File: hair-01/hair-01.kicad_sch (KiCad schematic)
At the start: 28 parts, among them J1 TYPE-C-31-M-12, Q1 BC847, Q2 BC847, SW1 SW_Push, U1 ESP-12F, U2 AP2112K-3.3, U3 CP2102N-Axx-xQFN24

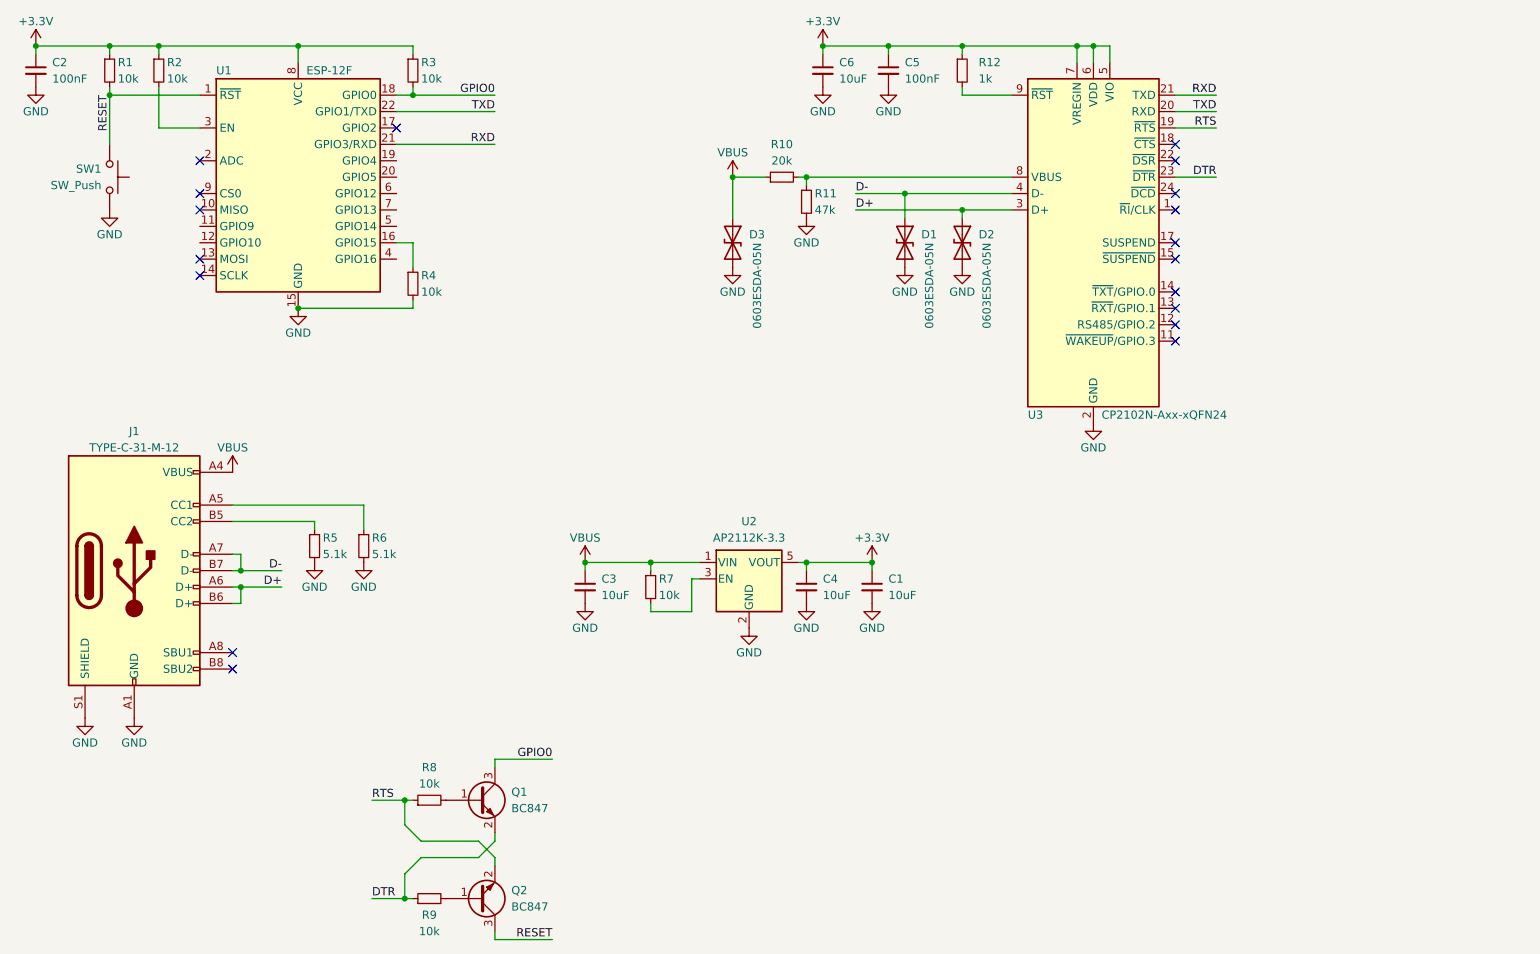
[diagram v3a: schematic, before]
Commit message: hair-01: Add TSMP58000
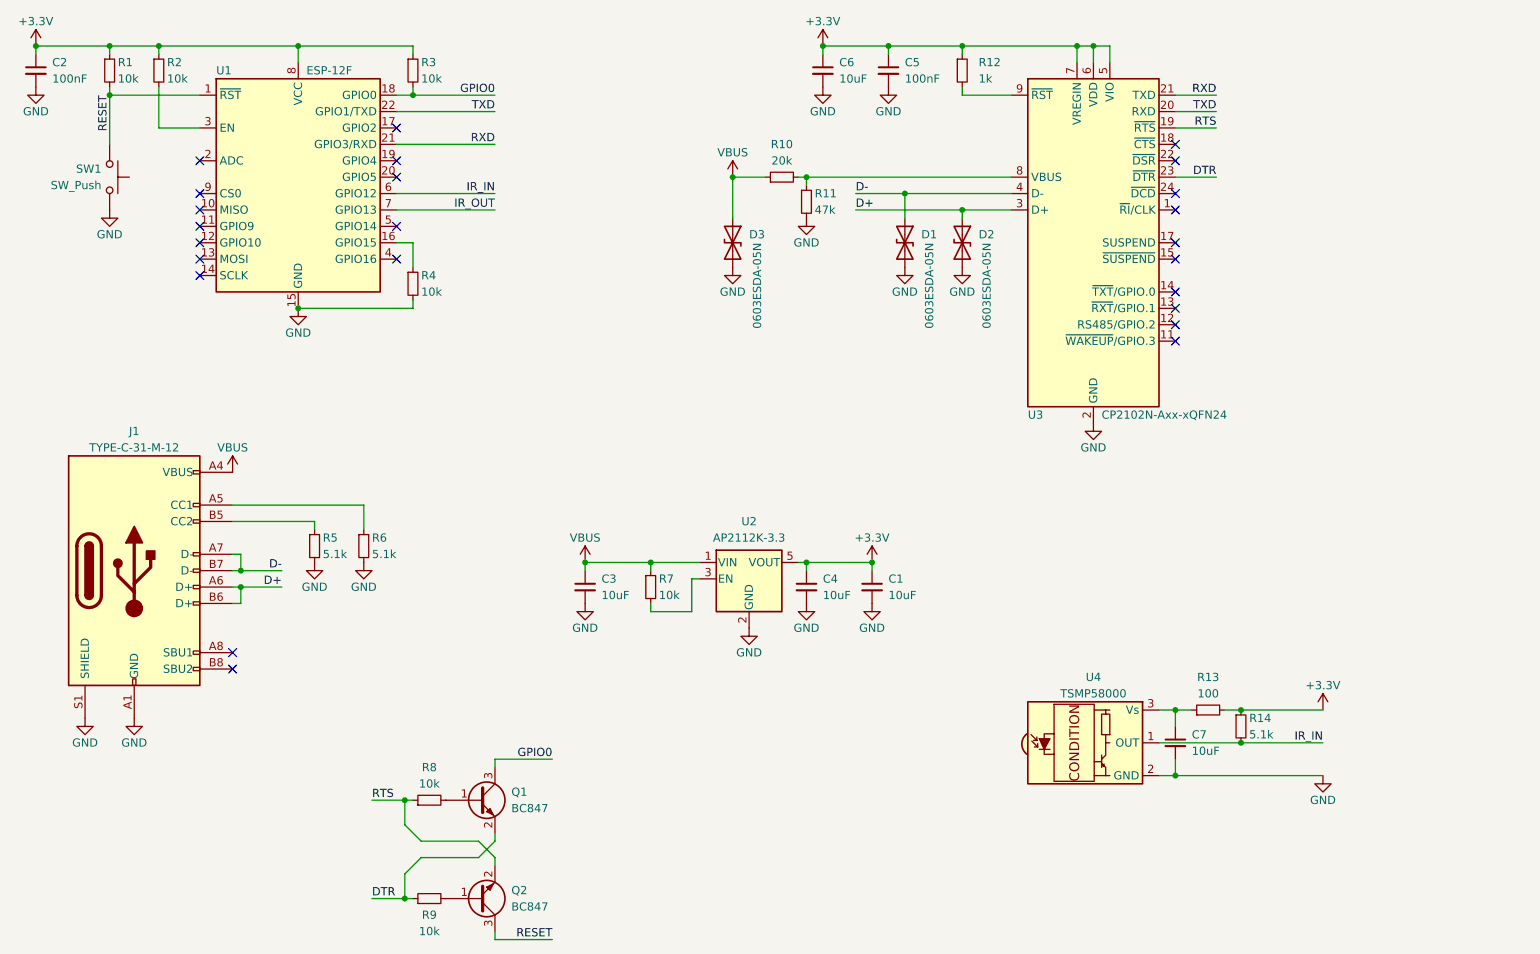
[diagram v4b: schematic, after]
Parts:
- added C7: 10uF, Capacitor_SMD:C_1206_3216Metric, symbol Device:C_Small
- added R13: 100, Resistor_SMD:R_0603_1608Metric, symbol Device:R_Small
- added R14: 5.1k, Resistor_SMD:R_0603_1608Metric, symbol Device:R_Small
- added U4: TSMP58000, OptoDevice:Vishay_MINICAST-3Pin, symbol Interface_Optical:TSMP58000
- C2, C5: footprint Capacitor_SMD:C_0805_2012Metric -> Capacitor_SMD:C_0603_1608Metric; LCSC C49678 -> C14663
- Q1, Q2: LCSC C2762211 -> C2150
- R1, R2, R3, R4, R7, R8, R9: footprint Resistor_SMD:R_0805_2012Metric -> Resistor_SMD:R_0603_1608Metric; LCSC C17414 -> C25804
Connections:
- net +3V3: now also R13.2, R14.1
- net GND: now also C7.2, U4.2 (GND)
- net IR_IN: now reaches U1.6 (GPIO12)
- net IR_IN: now also R14.2, U4.1 (OUT)
- net IR_OUT: now reaches U1.7 (GPIO13)
- new net: C7.1, R13.1, U4.3 (Vs)
- no-connect marks 18 -> 24

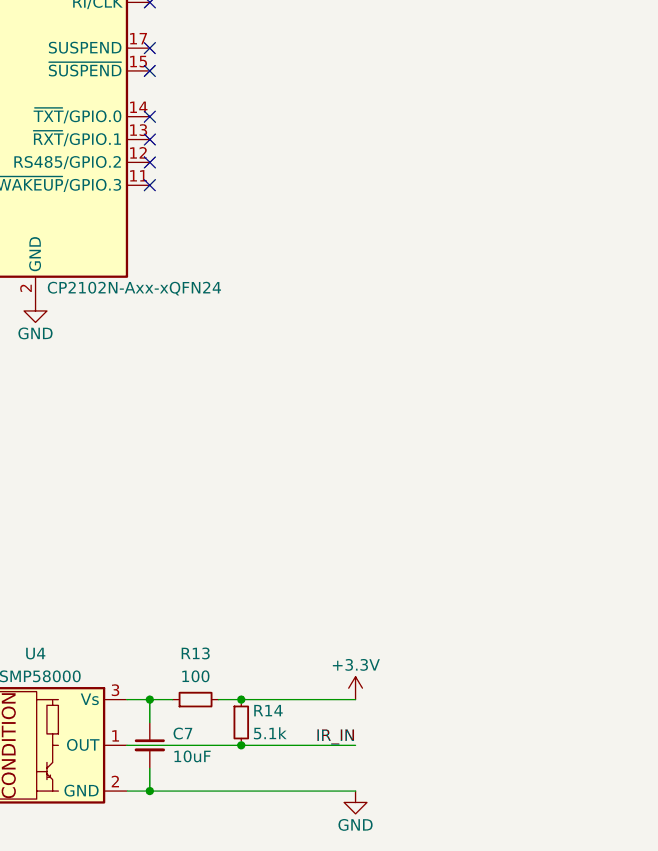
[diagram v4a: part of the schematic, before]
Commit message: hair-01: Add IR output
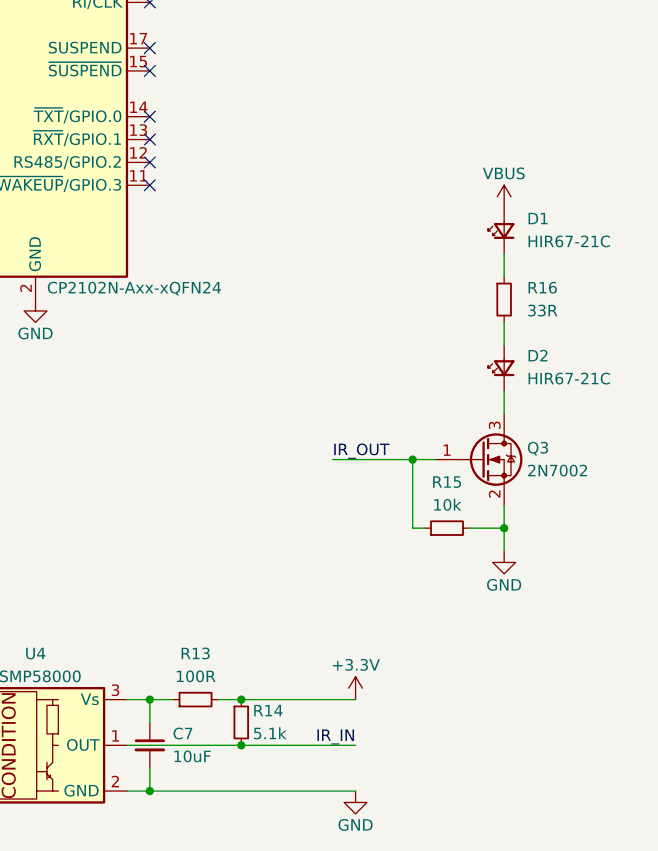
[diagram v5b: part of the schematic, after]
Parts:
- added D1, D2: HIR67-21C, LED_SMD:LED_1210_3225Metric_Pad1.42x2.65mm_HandSolder, symbol Device:LED_Small
- added Q3: 2N7002, Package_TO_SOT_SMD:SOT-23, symbol Transistor_FET:2N7002
- added R15: 10k, Resistor_SMD:R_0603_1608Metric, symbol Device:R_Small
- added R16: 33R, Resistor_SMD:R_1206_3216Metric, symbol Device:R_Small
- R13: value 100 -> 100R
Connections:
- net GND: now also Q3.2 (S), R15.2
- net IR_OUT: now also Q3.1 (G), R15.1
- net VBUS: now also D1.2 (A)
- new net: D1.1 (K), R16.1
- new net: D2.2 (A), R16.2
- new net: D2.1 (K), Q3.3 (D)

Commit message: hair-01: Fix small naming mistake
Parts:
- renumbered D1 to D4, D2 to D5
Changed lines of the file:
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@@
   (symbol (lib_id "Device:LED_Small") (at 251.46 104.14 90) (unit 1)
     (in_bom yes) (on_board yes) (fields_autoplaced)
-    (property "Reference" "D2" (id 0) (at 254 102.8064 90)
+    (property "Reference" "D5" (id 0) (at 254 102.8064 90)
       (effects (font (size 1.27 1.27)) (justify right))
     )
@@
   (symbol (lib_id "power:GND") (at 234.95 151.13 0) (unit 1)
     (in_bom yes) (on_board yes)
-    (property "Reference" "#PWR?" (id 0) (at 234.95 157.48 0)
+    (property "Reference" "#PWR0126" (id 0) (at 234.95 157.48 0)
       (effects (font (size 1.27 1.27)) hide)
     )
@@
   (symbol (lib_id "power:VBUS") (at 251.46 86.36 0) (unit 1)
     (in_bom yes) (on_board yes)
-    (property "Reference" "#PWR?" (id 0) (at 251.46 90.17 0)
+    (property "Reference" "#PWR0127" (id 0) (at 251.46 90.17 0)
       (effects (font (size 1.27 1.27)) hide)
     )
@@
   (symbol (lib_id "power:+3.3V") (at 234.95 140.97 0) (unit 1)
     (in_bom yes) (on_board yes)
-    (property "Reference" "#PWR?" (id 0) (at 234.95 144.78 0)
+    (property "Reference" "#PWR0125" (id 0) (at 234.95 144.78 0)
       (effects (font (size 1.27 1.27)) hide)
     )
@@
   (symbol (lib_id "power:GND") (at 251.46 124.46 0) (unit 1)
     (in_bom yes) (on_board yes)
-    (property "Reference" "#PWR?" (id 0) (at 251.46 130.81 0)
+    (property "Reference" "#PWR0128" (id 0) (at 251.46 130.81 0)
       (effects (font (size 1.27 1.27)) hide)
     )
@@
   (symbol (lib_id "Device:LED_Small") (at 251.46 88.9 90) (unit 1)
     (in_bom yes) (on_board yes) (fields_autoplaced)
-    (property "Reference" "D1" (id 0) (at 254 87.5664 90)
+    (property "Reference" "D4" (id 0) (at 254 87.5664 90)
       (effects (font (size 1.27 1.27)) (justify right))
     )
@@
       (reference "#PWR0124") (unit 1) (value "GND") (footprint "")
     )
+    (path "/809f19e5-adbf-43c9-ac69-4b9242bfc168"
+      (reference "#PWR0125") (unit 1) (value "+3.3V") (footprint "")
+    )
     (path "/56c37fb4-8586-41a1-bb86-a336aad0691f"
-      (reference "#PWR?") (unit 1) (value "GND") (footprint "")
+      (reference "#PWR0126") (unit 1) (value "GND") (footprint "")
     )
     (path "/6d3c885f-f204-4303-8718-76b0888b083a"
-      (reference "#PWR?") (unit 1) (value "VBUS") (footprint "")
-    )
-    (path "/809f19e5-adbf-43c9-ac69-4b9242bfc168"
-      (reference "#PWR?") (unit 1) (value "+3.3V") (footprint "")
+      (reference "#PWR0127") (unit 1) (value "VBUS") (footprint "")
     )
     (path "/f70317a6-1871-43c4-85ae-861e13960494"
-      (reference "#PWR?") (unit 1) (value "GND") (footprint "")
+      (reference "#PWR0128") (unit 1) (value "GND") (footprint "")
     )
     (path "/e3e9735d-c510-487b-99b0-46bcb726e4b1"
@@
       (reference "D1") (unit 1) (value "0603ESDA-05N") (footprint "Diode_SMD:D_0603_1608Metric")
     )
-    (path "/ff2c165b-fcf1-4e49-a130-75315ee7c31f"
-      (reference "D1") (unit 1) (value "HIR67-21C") (footprint "LED_SMD:LED_1210_3225Metric_Pad1.42x2.65mm_HandSolder")
-    )
-    (path "/2f375a34-8f19-4e0e-9faa-8667ac532147"
-      (reference "D2") (unit 1) (value "HIR67-21C") (footprint "LED_SMD:LED_1210_3225Metric_Pad1.42x2.65mm_HandSolder")
-    )
     (path "/4b834fac-5506-4328-bf03-f80519218eb0"
       (reference "D2") (unit 1) (value "0603ESDA-05N") (footprint "Diode_SMD:D_0603_1608Metric")
@@
       (reference "D3") (unit 1) (value "0603ESDA-05N") (footprint "Diode_SMD:D_0603_1608Metric")
     )
+    (path "/ff2c165b-fcf1-4e49-a130-75315ee7c31f"
+      (reference "D4") (unit 1) (value "HIR67-21C") (footprint "LED_SMD:LED_1210_3225Metric_Pad1.42x2.65mm_HandSolder")
+    )
+    (path "/2f375a34-8f19-4e0e-9faa-8667ac532147"
+      (reference "D5") (unit 1) (value "HIR67-21C") (footprint "LED_SMD:LED_1210_3225Metric_Pad1.42x2.65mm_HandSolder")
+    )
     (path "/ddcc8b27-b0b1-4e05-a565-cdc8d0a9dd1e"

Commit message: hair-01: Specify correct footprint for CP2102N
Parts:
- U3: footprint Package_DFN_QFN:SiliconLabs_QFN-20-1EP_3x3mm_P0.5mm -> Package_DFN_QFN:QFN-24-1EP_4x4mm_P0.5mm_EP2.6x2.6mm
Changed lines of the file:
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@@
       (effects (font (size 1.27 1.27)) (justify left))
     )
-    (property "Footprint" "Package_DFN_QFN:SiliconLabs_QFN-20-1EP_3x3mm_P0.5mm" (id 2) (at 231.14 95.25 0)
+    (property "Footprint" "Package_DFN_QFN:QFN-24-1EP_4x4mm_P0.5mm_EP2.6x2.6mm" (id 2) (at 231.14 95.25 0)
       (effects (font (size 1.27 1.27)) hide)
     )
@@
     )
     (path "/57a35f7e-1eec-4bce-82d8-651d3f20ac22"
-      (reference "U3") (unit 1) (value "CP2102N-Axx-xQFN24") (footprint "Package_DFN_QFN:SiliconLabs_QFN-20-1EP_3x3mm_P0.5mm")
+      (reference "U3") (unit 1) (value "CP2102N-Axx-xQFN24") (footprint "Package_DFN_QFN:QFN-24-1EP_4x4mm_P0.5mm_EP2.6x2.6mm")
     )
     (path "/4a2b5cd4-5349-4db9-bad8-5838bfe646c9"

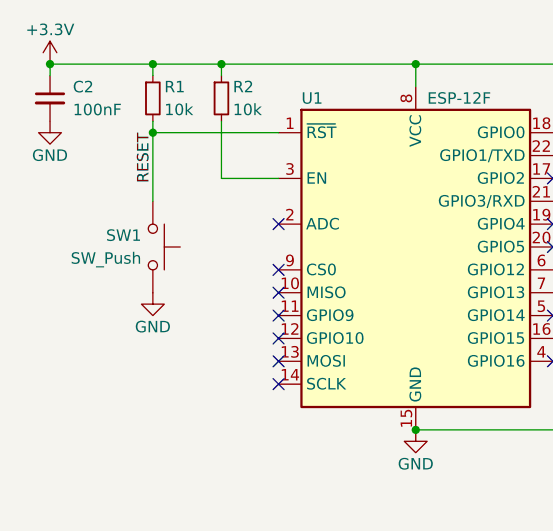
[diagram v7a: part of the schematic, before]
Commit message: hair-01: Rotate reset switch
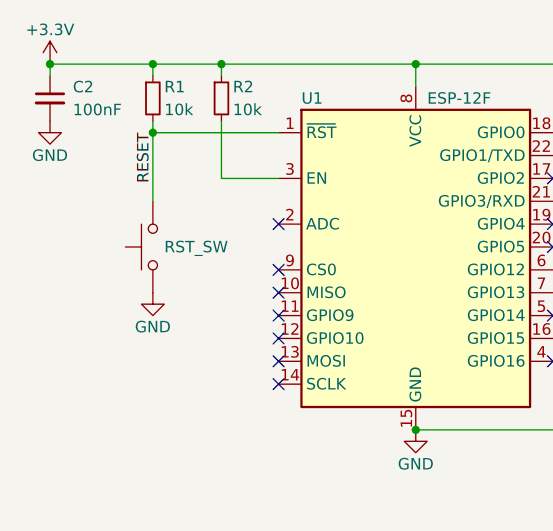
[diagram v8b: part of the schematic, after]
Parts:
- renumbered SW1 to RST_SW
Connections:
- net GND: now also RST_SW.1; no longer RST_SW.2
- net RESET: now also RST_SW.2; no longer RST_SW.1
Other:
- moved on the sheet: RST_SW
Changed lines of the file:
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@@
   (junction (at 154.94 58.42) (diameter 0) (color 0 0 0 0)
   )
+  (junction (at 54.61 38.1) (diameter 0) (color 0 0 0 0)
+  )
+  (junction (at 67.31 121.92) (diameter 0) (color 0 0 0 0)
+  )
+  (junction (at 120.65 118.11) (diameter 0) (color 0 0 0 0)
+  )
+  (junction (at 170.18 60.96) (diameter 0) (color 0 0 0 0)
+  )
+  (junction (at 76.2 78.74) (diameter 0) (color 0 0 0 0)
+  )
+  (junction (at 76.2 38.1) (diameter 0) (color 0 0 0 0)
+  )
+  (junction (at 179.07 63.5) (diameter 0) (color 0 0 0 0)
+  )
   (junction (at 46.99 45.72) (diameter 0) (color 0 0 0 0)
-  )
-  (junction (at 54.61 38.1) (diameter 0) (color 0 0 0 0)
-  )
-  (junction (at 67.31 121.92) (diameter 0) (color 0 0 0 0)
-  )
-  (junction (at 120.65 118.11) (diameter 0) (color 0 0 0 0)
-  )
-  (junction (at 170.18 60.96) (diameter 0) (color 0 0 0 0)
-  )
-  (junction (at 76.2 78.74) (diameter 0) (color 0 0 0 0)
-  )
-  (junction (at 76.2 38.1) (diameter 0) (color 0 0 0 0)
-  )
-  (junction (at 179.07 63.5) (diameter 0) (color 0 0 0 0)
   )
   (junction (at 143.51 58.42) (diameter 0) (color 0 0 0 0)
@@
     (stroke (width 0) (type default) (color 0 0 0 0))
   )
+  (wire (pts (xy 46.99 45.72) (xy 46.99 53.34))
+    (stroke (width 0) (type default) (color 0 0 0 0))
+  )
   (wire (pts (xy 170.18 60.96) (xy 186.69 60.96))
     (stroke (width 0) (type default) (color 0 0 0 0))
@@
   )
   (wire (pts (xy 137.16 125.73) (xy 137.16 120.65))
-    (stroke (width 0) (type default) (color 0 0 0 0))
-  )
-  (wire (pts (xy 46.99 45.72) (xy 46.99 53.34))
     (stroke (width 0) (type default) (color 0 0 0 0))
   )
@@
     (pin "2")
   )
-  (symbol (lib_id "Switch:SW_Push") (at 46.99 58.42 270) (unit 1)
-    (in_bom yes) (on_board yes)
-    (property "Reference" "SW1" (id 0) (at 45.72 57.15 90)
+  (symbol (lib_id "Switch:SW_Push") (at 46.99 58.42 90) (unit 1)
+    (in_bom yes) (on_board yes)
+    (property "Reference" "RST_SW" (id 0) (at 48.26 58.42 90)
       (effects (font (size 1.27 1.27)) (justify right))
     )
-    (property "Value" "SW_Push" (id 1) (at 45.72 59.69 90)
-      (effects (font (size 1.27 1.27)) (justify right))
-    )
-    (property "Footprint" "Button_Switch_SMD:SW_Push_1P1T-MP_NO_Horizontal_Alps_SKRTLAE010" (id 2) (at 52.07 58.42 0)
-      (effects (font (size 1.27 1.27)) hide)
-    )
-    (property "Datasheet" "~" (id 3) (at 52.07 58.42 0)
+    (property "Value" "SW_Push" (id 1) (at 48.26 57.15 90)
+      (effects (font (size 1.27 1.27)) (justify right) hide)
+    )
+    (property "Footprint" "Button_Switch_SMD:SW_Push_1P1T-MP_NO_Horizontal_Alps_SKRTLAE010" (id 2) (at 41.91 58.42 0)
+      (effects (font (size 1.27 1.27)) hide)
+    )
+    (property "Datasheet" "~" (id 3) (at 41.91 58.42 0)
       (effects (font (size 1.27 1.27)) hide)
     )
@@
     )
     (path "/74adff30-1759-49f6-8036-03af26649b8b"
-      (reference "SW1") (unit 1) (value "SW_Push") (footprint "Button_Switch_SMD:SW_Push_1P1T-MP_NO_Horizontal_Alps_SKRTLAE010")
+      (reference "RST_SW") (unit 1) (value "SW_Push") (footprint "Button_Switch_SMD:SW_Push_1P1T-MP_NO_Horizontal_Alps_SKRTLAE010")
     )
     (path "/5778953d-c3f1-4eab-88e0-47485d04ab27"
